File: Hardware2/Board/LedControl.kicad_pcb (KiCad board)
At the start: 2 copper layers, 69 x 50 mm, 124 parts, among them J2 Jumper, J3 Jumper, J4 J, J5 J, J6 J, P1 USB_OTG, P10 TP, P11 2059-302, P12 DISPLAY, P13 TP, P14 Conn_01x03, P15 TP, P16 2059-302, P17 2059-302, P18 CONN_01X03, P19 CONN_01X03, P2 TP, P20 TP, P21 TP, P22 TP, P23 TP, P24 2060-452, P25 2060-452, P26 TP, P27 TP, P28 2060-452, P29 2059-302, P3 TP, P30 LED_Strip, P31 LED_Strip, P32 TP, P33 TP, P34 TP, P4 TP, P5 2059-302, P6 TP, P7 TP, P8 Micro_SD, P9 TP, SW1 PEC12R-4215F-S0024, SW2 PEC12R-4215F-S0024, U1 STM32L433CCUx, U2 SP485CN, U3 SP485CN, U4 SP485CN, U5 TPS82130, U6 LP2985IM5-3.3, U7 TPS82130, U8 SP485CN, U9 TPS82130, X1 IQXO/7X

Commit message: LED strip power supply below strip
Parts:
- removed the C11 at (75.3, 86.3)
- removed the C11 at (82.3, 86.3)
- removed the C11 at (89.3, 86.3)
- removed the C11 at (96.3, 86.3)
- removed the C11 at (103.2, 86.3)
- removed the C12 at (75.2, 92.2)
- removed the C12 at (82.2, 92.2)
- removed the C12 at (89.2, 92.2)
- removed the C12 at (96.2, 92.2)
- removed the C12 at (103.0, 92.2)
- removed the P31 at (72.1, 96.5)
- removed the P31 at (79.1, 96.5)
- removed the P31 at (86.1, 96.5)
- removed the P31 at (93.1, 96.5)
- removed the P31 at (100.0, 96.5)
- removed the R16 at (75.7, 94.2)
- removed the R16 at (82.7, 94.2)
- removed the R16 at (89.7, 94.2)
- removed the R16 at (96.7, 94.2)
- removed the R16 at (103.6, 94.2)
- removed the R17 at (75.7, 96.0)
- removed the R17 at (82.7, 96.0)
- removed the R17 at (89.7, 96.0)
- removed the R17 at (96.7, 96.0)
- removed the R17 at (103.6, 96.0)
- removed the U9 at (74.9, 89.3)
- removed the U9 at (81.9, 89.3)
- removed the U9 at (88.9, 89.3)
- removed the U9 at (95.9, 89.3)
- removed the U9 at (102.8, 89.3)
- added C11: 10u, Capacitor_SMD:C_1206_3216Metric, F.Cu at (75.6, 96.6)
- added C11: 10u, Capacitor_SMD:C_1206_3216Metric, F.Cu at (82.6, 96.6)
- added C11: 10u, Capacitor_SMD:C_1206_3216Metric, F.Cu at (89.6, 96.6)
- added C11: 10u, Capacitor_SMD:C_1206_3216Metric, F.Cu at (96.6, 96.6)
- added C11: 10u, Capacitor_SMD:C_1206_3216Metric, F.Cu at (103.6, 96.6)
- added C12: 22u, Capacitor_SMD:C_0805_2012Metric, F.Cu at (75.0, 90.6)
- added C12: 22u, Capacitor_SMD:C_0805_2012Metric, F.Cu at (82.0, 90.6)
- added C12: 22u, Capacitor_SMD:C_0805_2012Metric, F.Cu at (89.0, 90.6)
- added C12: 22u, Capacitor_SMD:C_0805_2012Metric, F.Cu at (96.0, 90.6)
- added C12: 22u, Capacitor_SMD:C_0805_2012Metric, F.Cu at (103.0, 90.6)
- added P31: LED_Strip, LedControl:LED_Strip, F.Cu at (72.0, 97.5)
- added P31: LED_Strip, LedControl:LED_Strip, F.Cu at (79.0, 97.5)
- added P31: LED_Strip, LedControl:LED_Strip, F.Cu at (86.0, 97.5)
- added P31: LED_Strip, LedControl:LED_Strip, F.Cu at (93.0, 97.5)
- added P31: LED_Strip, LedControl:LED_Strip, F.Cu at (100.0, 97.5)
- added R16: 52k3, Resistor_SMD:R_0603_1608Metric, F.Cu at (74.8, 88.9)
- added R16: 52k3, Resistor_SMD:R_0603_1608Metric, F.Cu at (81.8, 88.9)
- added R16: 52k3, Resistor_SMD:R_0603_1608Metric, F.Cu at (88.8, 88.9)
- added R16: 52k3, Resistor_SMD:R_0603_1608Metric, F.Cu at (95.8, 88.9)
- added R16: 52k3, Resistor_SMD:R_0603_1608Metric, F.Cu at (102.8, 88.9)
- added R17: 10k, Resistor_SMD:R_0603_1608Metric, F.Cu at (74.3, 86.8)
- added R17: 10k, Resistor_SMD:R_0603_1608Metric, F.Cu at (81.3, 86.8)
- added R17: 10k, Resistor_SMD:R_0603_1608Metric, F.Cu at (88.3, 86.8)
- added R17: 10k, Resistor_SMD:R_0603_1608Metric, F.Cu at (95.3, 86.8)
- added R17: 10k, Resistor_SMD:R_0603_1608Metric, F.Cu at (102.3, 86.8)
- added U9: TPS82130, LedControl:TPS82130, F.Cu at (75.2, 93.5)
- added U9: TPS82130, LedControl:TPS82130, F.Cu at (82.2, 93.5)
- added U9: TPS82130, LedControl:TPS82130, F.Cu at (89.2, 93.5)
- added U9: TPS82130, LedControl:TPS82130, F.Cu at (96.2, 93.5)
- added U9: TPS82130, LedControl:TPS82130, F.Cu at (103.2, 93.5)
- D2, D3: value SS 12L -> SD1206S020S1R0
- D4: value D -> SD1206S020S1R0
- DIVIDER2: value Divider_21mm -> Divider_22mm; footprint LedControl:Divider_21mm -> LedControl:Divider_22mm
- P14: value Conn_01x03 -> TMM-103-03-G-S
- P30: footprint LedControl:LED_Strip_Start -> LedControl:LED_Strip
- moved C11 10.3 mm to (110.6, 96.6), turned to 180 degrees
- moved C9 10.3 mm to (117.6, 96.6), turned to 180 degrees
- moved R17 9.29 mm to (109.3, 86.8), turned to 90 degrees
- moved U8 8.61 mm to (122.0, 86.8)
- moved P29 8.50 mm to (130.0, 87.0)
- moved R11 7.31 mm to (77.5, 122.9), turned to 0 degrees
- moved P28 5.50 mm to (128.0, 94.0)
- moved R16 5.36 mm to (109.8, 88.9), turned to 180 degrees
- moved U7 4.22 mm to (117.2, 93.5), turned to 180 degrees
- moved U9 4.22 mm to (110.2, 93.5), turned to 180 degrees
- moved R15 3.82 mm to (116.3, 86.8)
- moved R14 3.67 mm to (116.8, 88.9), turned to 180 degrees
- moved C10 2.01 mm to (117.0, 90.6), turned to 0 degrees
- moved C12 1.55 mm to (110.0, 90.6), turned to 0 degrees
- moved DIVIDER1 1.00 mm to (77.0, 99.0)
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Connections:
- C10 pad 1: Net-(C10-Pad1) -> +5VD
- C10 pad 2: Net-(C10-Pad2) -> GNDD
- C11 pad 2: Net-(C10-Pad2) -> GNDD
- C12 pad 1: Net-(C10-Pad1) -> +5VD
- C12 pad 2: Net-(C10-Pad2) -> GNDD
- C9 pad 2: Net-(C10-Pad2) -> GNDD
- P28 pad 1: Net-(C10-Pad2) -> Net-(C11-Pad1)
- P28 pad 2: Net-(C11-Pad1) -> GNDD
- P30 pad 1: Net-(C10-Pad2) -> Net-(C11-Pad1)
- P30 pad 2: Net-(P30-Pad2) -> GNDD
- P30 pad 3: Net-(C10-Pad1) -> GNDD
- P30 pad 4: Net-(C10-Pad2) -> Net-(P30-Pad4)
- P30 pad 5: Net-(C11-Pad1) -> +5VD
- P31 pad 1: Net-(C10-Pad2) -> Net-(C11-Pad1)
- P31 pad 2: Net-(P30-Pad2) -> GNDD
- P31 pad 3: Net-(C10-Pad1) -> GNDD
- P31 pad 4: Net-(C10-Pad2) -> Net-(P30-Pad4)
- P31 pad 5: Net-(C11-Pad1) -> +5VD
- R14 pad 1: Net-(C10-Pad1) -> +5VD
- R15 pad 2: Net-(C10-Pad2) -> GNDD
- R16 pad 1: Net-(C10-Pad1) -> +5VD
- R17 pad 2: Net-(C10-Pad2) -> GNDD
- U7 pad 3: Net-(C10-Pad2) -> GNDD
- U7 pad 4: Net-(C10-Pad1) -> +5VD
- U7 pad 5: Net-(C10-Pad1) -> +5VD
- U7 pad 9: Net-(C10-Pad2) -> GNDD
- U8 pad 1: Net-(P30-Pad2) -> Net-(P30-Pad4)
- U8 pad 2: Net-(C10-Pad2) -> GNDD
- U8 pad 3: Net-(C10-Pad2) -> GNDD
- U8 pad 4: Net-(C10-Pad2) -> GNDD
- U8 pad 5: Net-(C10-Pad2) -> GNDD
- U8 pad 8: Net-(C10-Pad1) -> +5VD
- U9 pad 3: Net-(C10-Pad2) -> GNDD
- U9 pad 4: Net-(C10-Pad1) -> +5VD
- U9 pad 5: Net-(C10-Pad1) -> +5VD
- U9 pad 9: Net-(C10-Pad2) -> GNDD
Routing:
- net Net-(C10-Pad2): track 149.8 -> 0.00 mm, vias 12 -> 0
- net GNDD: track 0.00 -> 127.2 mm, vias 0 -> 10
- net +5VD: track 0.00 -> 82.3 mm, vias 0 -> 1
- net (no net): track 434.8 -> 485.6 mm, vias 30 -> 15
- net Net-(C10-Pad1): track 49.3 -> 0.00 mm, vias 4 -> 0
- net Net-(P30-Pad4): track 0.00 -> 16.9 mm, vias 0 -> 1
- net Net-(P30-Pad2): track 13.6 -> 0.00 mm
- net Net-(C11-Pad1): track 48.2 -> 56.2 mm
- net ENC1_SW: track 121.5 -> 128.1 mm
- net Net-(R14-Pad2): track 3.02 -> 6.70 mm
- net Net-(R16-Pad2): track 14.5 -> 13.4 mm
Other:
- board size 69 x 50 mm -> 70 x 51 mm
- board text added: "B A GND VCC"

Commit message: Add CAN bus
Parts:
- removed the C11 at (75.6, 96.6)
- removed the C11 at (82.6, 96.6)
- removed the C11 at (89.6, 96.6)
- removed the C11 at (96.6, 96.6)
- removed the C11 at (103.6, 96.6)
- removed the C12 at (75.0, 90.6)
- removed the C12 at (82.0, 90.6)
- removed the C12 at (89.0, 90.6)
- removed the C12 at (96.0, 90.6)
- removed the C12 at (103.0, 90.6)
- removed J6: J, LedControl:Jumper
- removed the P10 at (98.2, 115.0)
- removed the P31 at (72.0, 97.5)
- removed the P31 at (79.0, 97.5)
- removed the P31 at (86.0, 97.5)
- removed the P31 at (93.0, 97.5)
- removed the P31 at (100.0, 97.5)
- removed the R16 at (74.8, 88.9)
- removed the R16 at (81.8, 88.9)
- removed the R16 at (88.8, 88.9)
- removed the R16 at (95.8, 88.9)
- removed the R16 at (102.8, 88.9)
- removed the R17 at (74.3, 86.8)
- removed the R17 at (81.3, 86.8)
- removed the R17 at (88.3, 86.8)
- removed the R17 at (95.3, 86.8)
- removed the R17 at (102.3, 86.8)
- removed SLOT: Slot_15x2mm, LedControl:Slot_15x2mm
- removed the U9 at (75.2, 93.5)
- removed the U9 at (82.2, 93.5)
- removed the U9 at (89.2, 93.5)
- removed the U9 at (96.2, 93.5)
- removed the U9 at (103.2, 93.5)
- added C11: 10u, Capacitor_SMD:C_1206_3216Metric, F.Cu at (76.6, 96.6)
- added C11: 10u, Capacitor_SMD:C_1206_3216Metric, F.Cu at (83.4, 96.6)
- added C11: 10u, Capacitor_SMD:C_1206_3216Metric, F.Cu at (90.2, 96.6)
- added C11: 10u, Capacitor_SMD:C_1206_3216Metric, F.Cu at (97.0, 96.6)
- added C11: 10u, Capacitor_SMD:C_1206_3216Metric, F.Cu at (103.8, 96.6)
- added C12: 22u, Capacitor_SMD:C_0805_2012Metric, F.Cu at (76.2, 90.6)
- added C12: 22u, Capacitor_SMD:C_0805_2012Metric, F.Cu at (83.0, 90.6)
- added C12: 22u, Capacitor_SMD:C_0805_2012Metric, F.Cu at (89.8, 90.6)
- added C12: 22u, Capacitor_SMD:C_0805_2012Metric, F.Cu at (96.6, 90.6)
- added C12: 22u, Capacitor_SMD:C_0805_2012Metric, F.Cu at (103.4, 90.6)
- added C15: 100n, Capacitor_SMD:C_0603_1608Metric, F.Cu at (128.6, 112.2)
- added C16: 100n, Capacitor_SMD:C_0603_1608Metric, B.Cu at (111.1, 118.7)
- added C17: 100n, Capacitor_SMD:C_0603_1608Metric, B.Cu at (109.6, 118.7)
- added D5: SD1206S020S1R0, Diode_SMD:D_1206_3216Metric, B.Cu at (96.2, 113.8)
- added D6: SD1206S020S1R0, Diode_SMD:D_1206_3216Metric, B.Cu at (98.6, 111.2)
- added J7: Jumper, LedControl:Jumper, B.Cu at (77.0, 113.7)
- added P31: LED_Strip, LedControl:LED_Strip, F.Cu at (73.2, 97.5)
- added P31: LED_Strip, LedControl:LED_Strip, F.Cu at (80.0, 97.5)
- added P31: LED_Strip, LedControl:LED_Strip, F.Cu at (86.8, 97.5)
- added P31: LED_Strip, LedControl:LED_Strip, F.Cu at (93.6, 97.5)
- added P31: LED_Strip, LedControl:LED_Strip, F.Cu at (100.4, 97.5)
- added P35: 2060-452, LedControl:WAGO_2060-452, F.Cu at (69.0, 90.9)
- added P36: TP, LedControl:Pad, B.Cu at (93.8, 131.6)
- added P38: TP, LedControl:Pad, B.Cu at (100.8, 104.3)
- added P39: TP, LedControl:Pad, B.Cu at (100.1, 133.2)
- added P40: TP, LedControl:Pad, B.Cu at (102.2, 104.3)
- added P41: TP, LedControl:Pad, B.Cu at (76.6, 130.8)
- added P42: TP, LedControl:Pad, B.Cu at (76.6, 132.4)
- added P43: TP, LedControl:Pad, B.Cu at (76.6, 134.0)
- added P44: TP, LedControl:Pad, B.Cu at (98.0, 104.3)
- added P8: 2059-302, LedControl:WAGO_2059-302, F.Cu at (68.0, 105.0)
- added Q1: DMG1012UW, Package_TO_SOT_SMD:SOT-323_SC-70, B.Cu at (99.0, 115.2)
- added Q2: DMG1012UW, Package_TO_SOT_SMD:SOT-323_SC-70, B.Cu at (101.4, 112.6)
- added R16: 52k3, Resistor_SMD:R_0603_1608Metric, F.Cu at (76.0, 88.9)
- added R16: 52k3, Resistor_SMD:R_0603_1608Metric, F.Cu at (82.8, 88.9)
- added R16: 52k3, Resistor_SMD:R_0603_1608Metric, F.Cu at (89.6, 88.9)
- added R16: 52k3, Resistor_SMD:R_0603_1608Metric, F.Cu at (96.4, 88.9)
- added R16: 52k3, Resistor_SMD:R_0603_1608Metric, F.Cu at (103.2, 88.9)
- added R17: 10k, Resistor_SMD:R_0603_1608Metric, F.Cu at (75.5, 86.8)
- added R17: 10k, Resistor_SMD:R_0603_1608Metric, F.Cu at (82.3, 86.8)
- added R17: 10k, Resistor_SMD:R_0603_1608Metric, F.Cu at (89.1, 86.8)
- added R17: 10k, Resistor_SMD:R_0603_1608Metric, F.Cu at (95.9, 86.8)
- added R17: 10k, Resistor_SMD:R_0603_1608Metric, F.Cu at (102.7, 86.8)
- added R22: 390R, Resistor_SMD:R_0603_1608Metric, F.Cu at (111.6, 121.1)
- added R23: 120R, Resistor_SMD:R_1206_3216Metric, B.Cu at (92.0, 109.0)
- added R24: 120R, Resistor_SMD:R_1206_3216Metric, B.Cu at (92.0, 111.2)
- added R25: 10k, Resistor_SMD:R_0603_1608Metric, B.Cu at (110.4, 111.1)
- added R26: 120R, Resistor_SMD:R_1206_3216Metric, B.Cu at (110.7, 114.9)
- added R27: 10k, Resistor_SMD:R_0603_1608Metric, B.Cu at (108.8, 111.1)
- added R28: 120R, Resistor_SMD:R_1206_3216Metric, B.Cu at (108.5, 114.9)
- added R29: 10k, Resistor_SMD:R_0603_1608Metric, F.Cu at (128.2, 129.0)
- added U10: SP485CN, Package_SO:SOIC-8_3.9x4.9mm_P1.27mm, B.Cu at (92.0, 104.1)
- added U9: TPS82130, LedControl:TPS82130, F.Cu at (76.4, 93.5)
- added U9: TPS82130, LedControl:TPS82130, F.Cu at (83.2, 93.5)
- added U9: TPS82130, LedControl:TPS82130, F.Cu at (90.0, 93.5)
- added U9: TPS82130, LedControl:TPS82130, F.Cu at (96.8, 93.5)
- added U9: TPS82130, LedControl:TPS82130, F.Cu at (103.6, 93.5)
- J2: footprint LedControl:Jumper3 -> LedControl:Jumper; moved to F.Cu
- J3: footprint LedControl:Jumper -> LedControl:Jumper3; moved to F.Cu
- J4, J5: value J -> Jumper; footprint LedControl:Jumper -> LedControl:Jumper3; moved to B.Cu
- P11: value 2059-302 -> Header; footprint LedControl:WAGO_2059-302 -> Connector_PinHeader_2.54mm:PinHeader_1x04_P2.54mm_Vertical
- P14, P18, SW1, SW2: moved to F.Cu
- P15, P17, R5, U3: moved to B.Cu
- P16: value 2059-302 -> TP; footprint LedControl:WAGO_2059-302 -> LedControl:Pad; moved to B.Cu
- P19: value CONN_01X03 -> TP; footprint Connector_PinHeader_2.54mm:PinHeader_1x03_P2.54mm_Vertical -> LedControl:Pad
- P2, P3, P4: value TP -> 2059-302; footprint LedControl:Pad -> LedControl:WAGO_2059-302; moved to F.Cu
- P6, P7, P9: value TP -> 2059-302; footprint LedControl:Pad -> LedControl:WAGO_2059-302
- R19: value 52k3 -> 10k
- R20: value 10k -> 52k3
- R4, R6: value 120R -> 390R; footprint Resistor_SMD:R_1206_3216Metric -> Resistor_SMD:R_0603_1608Metric; moved to B.Cu
- R8: value 120R -> 10k; footprint Resistor_SMD:R_1206_3216Metric -> Resistor_SMD:R_0603_1608Metric
- U2: value SP485CN -> SN65HVD230
- moved C1 55.8 mm to (70.2, 129.0), turned to 180 degrees
- moved R10 52.0 mm to (66.2, 118.8), turned to 90 degrees
- moved P14 49.8 mm to (129.8, 133.8), turned to 90 degrees
- moved J4 49.1 mm to (125.1, 113.4), turned to 270 degrees
- moved U4 48.1 mm to (71.2, 132.4), turned to 180 degrees
- moved R9 45.4 mm to (68.4, 118.8), turned to 90 degrees
- moved P19 44.4 mm to (114.8, 130.9)
- moved R11 40.8 mm to (117.4, 131.5), turned to 180 degrees
- moved P4 37.1 mm to (120.0, 105.0), turned to 270 degrees
- moved P17 34.0 mm to (80.0, 105.0)
- moved P6 31.7 mm to (114.0, 105.0), turned to 270 degrees
- moved P18 30.2 mm to (67.2, 123.2), turned to 0 degrees
- moved P3 27.0 mm to (126.0, 105.0), turned to 270 degrees
- moved P7 26.5 mm to (120.0, 105.0), turned to 270 degrees
- moved P2 26.2 mm to (114.0, 105.0)
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- renumbered P8 to P10
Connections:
- J2 pad 1: +3V3 -> GND
- J3 pad 2: Net-(J3-Pad2) -> +3V3
- J4 pad 1: Net-(D2-Pad2) -> Net-(J4-Pad1)
- J4 pad 2: VCC -> +3V3
- J5 pad 1: Net-(D3-Pad2) -> Net-(J5-Pad1)
- J5 pad 2: VCC -> +3V3
- P11 pad 1: Net-(J3-Pad1) -> GND
- P11 pad 2: Net-(P11-Pad2) -> SWDIO
- P14 pad 1: SWDCLK -> GND
- P14 pad 3: GND -> SWCLK
- P17 pad 1: Net-(P17-Pad1) -> Net-(J5-Pad1)
- P17 pad 2: Net-(P17-Pad2) -> GND
- P19 pad 1: GND -> Net-(P19-Pad1)
- P2 pad 1: Net-(P2-Pad1) -> CANL
- P21 pad 1: +3V3 -> +5V
- P22 pad 1: +5V -> +3V3
- P3 pad 1: Net-(P3-Pad1) -> CANL
- P4 pad 1: Net-(P4-Pad1) -> GND
- P5 pad 2: Net-(J2-Pad2) -> Net-(J3-Pad1)
- P6 pad 1: Net-(P6-Pad1) -> RS485A
- P7 pad 1: Net-(P7-Pad1) -> Net-(J4-Pad1)
- P9 pad 1: DISP_SCK -> STRIP2_A
- R10 pad 2: Net-(P17-Pad1) -> STRIP1_A
- R19 pad 1: Net-(D3-Pad2) -> U1
- R19 pad 2: U2 -> GND
- R2 pad 1: Net-(J3-Pad2) -> CANH
- R2 pad 2: Net-(P11-Pad2) -> CANL
- R20 pad 1: U1 -> Net-(D3-Pad2)
- R20 pad 2: GND -> U2
- R4 pad 1: Net-(P16-Pad1) -> +5V
- R4 pad 2: Net-(R4-Pad2) -> RS485A
- R5 pad 1: Net-(P16-Pad1) -> RS485A
- R5 pad 2: Net-(P16-Pad2) -> RS485B
- R6 pad 1: Net-(P16-Pad2) -> RS485B
- R6 pad 2: Net-(R6-Pad2) -> GND
- R8 pad 1: DEBUG_LED -> Net-(J2-Pad2)
- R8 pad 2: Net-(D1-Pad2) -> GND
- R9 pad 2: Net-(P17-Pad2) -> STRIP1_B
- SW1 pad : (no net) -> GND
- SW1 pad A: ENC1_CH2 -> ENC1_CH1
- SW1 pad B: ENC1_CH1 -> ENC1_CH2
- SW1 pad S1: +3V3 -> ENC1_SW
- SW1 pad S2: ENC1_SW -> +3V3
- SW2 pad : (no net) -> GND
- SW2 pad A: ENC2_CH2 -> ENC2_CH1
- SW2 pad B: ENC2_CH1 -> ENC2_CH2
- U1 pad 13: STRIP2_RX -> Net-(P13-Pad1)
- U1 pad 14: Net-(P13-Pad1) -> DEBUG_LED
- U1 pad 2: STRIP2_DE -> Net-(P19-Pad1)
- U1 pad 37: SWDCLK -> SWCLK
- U1 pad 39: Net-(P4-Pad1) -> Net-(P36-Pad1)
- U1 pad 40: Net-(P6-Pad1) -> Net-(P39-Pad1)
- U1 pad 45: Net-(P7-Pad1) -> CAN_RX
- U1 pad 46: DEBUG_LED -> CAN_TX
- U1 pad 6: Net-(P2-Pad1) -> Net-(P16-Pad1)
- U1 pad 7: Net-(P3-Pad1) -> NRST
- U2 pad 1: RS485_RX -> CAN_TX
- U2 pad 2: RS485_DE -> GND
- U2 pad 3: RS485_DE -> +3V3
- U2 pad 4: RS485_TX -> CAN_RX
- U2 pad 5: GND -> Net-(U2-Pad5)
- U2 pad 6: Net-(J3-Pad1) -> CANL
- U2 pad 7: Net-(P11-Pad2) -> CANH
- U2 pad 8: +5V -> Net-(J2-Pad2)
- U3 pad 1: STRIP2_RX -> RS485_RX
- U3 pad 2: STRIP2_DE -> RS485_DE
- U3 pad 3: STRIP2_DE -> RS485_DE
- U3 pad 4: STRIP2_TX -> RS485_TX
- U3 pad 6: Net-(R4-Pad2) -> RS485A
- U3 pad 7: Net-(R6-Pad2) -> RS485B
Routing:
- net ENC1_SW: track 128.1 -> 59.6 mm
- net STRIP2_TX: track 9.06 -> 59.0 mm, vias 0 -> 1
- net +5V: track 121.2 -> 169.0 mm, vias 7 -> 10
- net CAN_RX: track 0.00 -> 46.3 mm, vias 0 -> 2
- net CAN_TX: track 0.00 -> 41.0 mm, vias 0 -> 2
- net SWCLK: track 0.00 -> 40.0 mm, vias 0 -> 1
- net NRST: track 0.00 -> 34.3 mm, vias 0 -> 2
- net CANH: track 0.00 -> 33.7 mm, vias 0 -> 2
- net RS485B: track 0.00 -> 32.2 mm, vias 0 -> 2
- net SWDCLK: track 31.4 -> 0.00 mm, vias 2 -> 0
- net CANL: track 0.00 -> 31.4 mm
- net STRIP1_TTY_TX: track 66.6 -> 39.7 mm
- net GNDD: track 127.2 -> 153.8 mm, vias 10 -> 12
- net Net-(C11-Pad1): track 56.2 -> 82.7 mm, vias 3 -> 6
- net RS485A: track 0.00 -> 24.7 mm
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- removed copper zone on B.Cu, net Net-(D2-Pad2)
- removed copper zone on B.Cu, net Net-(D3-Pad2)
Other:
- board text added: "A B"
- board text added: "CAN H L"
- board text added: "D CL"
- board text added: "GND VCC"
- board text added: "R CL D"
- board text added: "RS485 B A"
- board text added: "STRIP2 B A GND 5V"
- board text added: "VCC G VCC GND"
- board text removed: "B A B A B A LED1 LED2 485"
- board text removed: "RS485 TERM"
- board text removed: "VCC GND VCC GND"
- board text removed: "VDD"

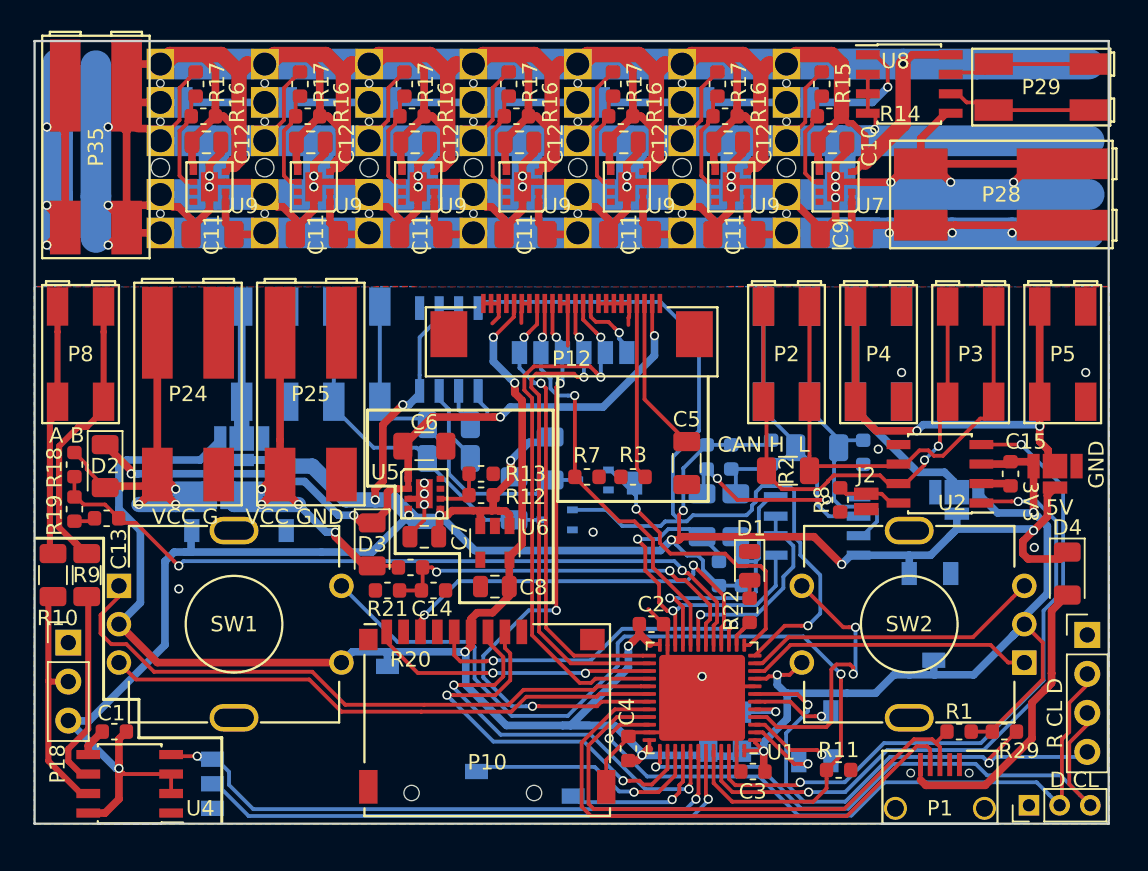
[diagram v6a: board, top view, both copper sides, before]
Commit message: USB and SD card at center
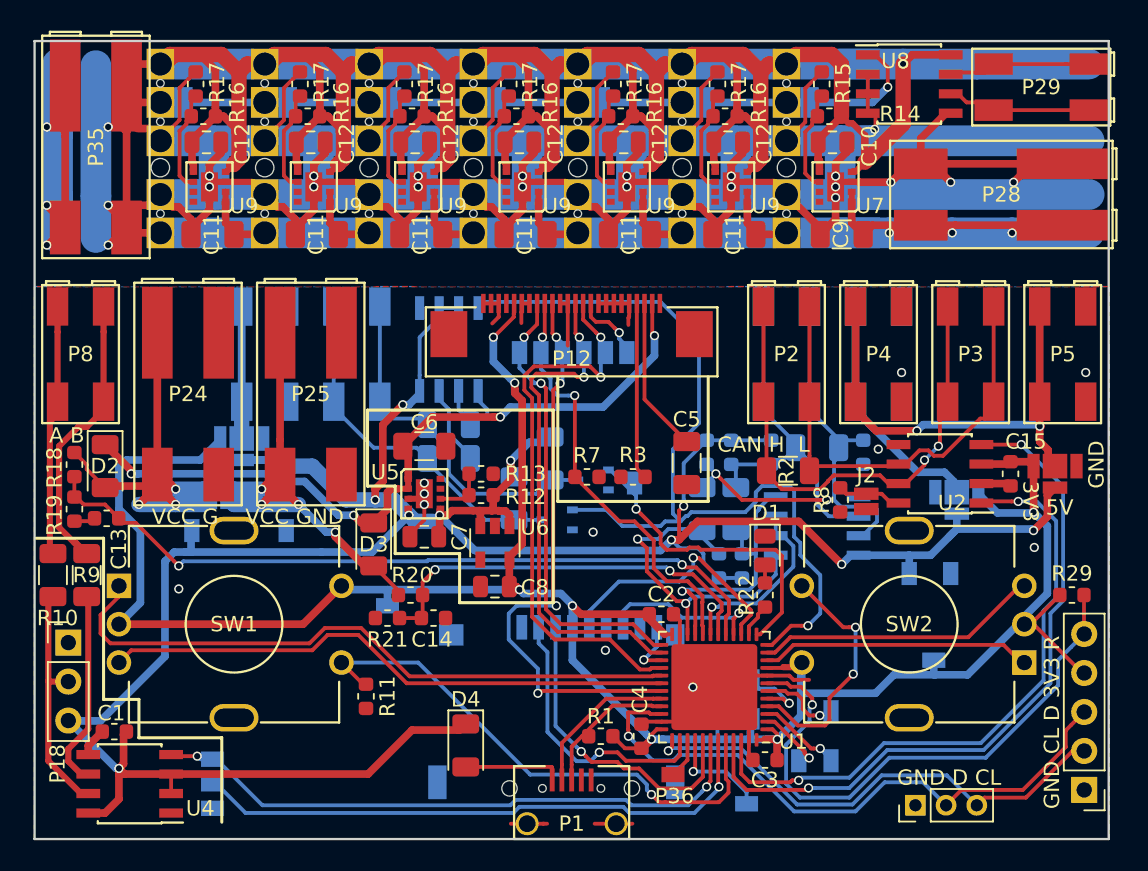
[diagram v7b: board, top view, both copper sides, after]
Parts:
- P10: moved to B.Cu
- P11: footprint Connector_PinHeader_2.54mm:PinHeader_1x04_P2.54mm_Vertical -> Connector_PinHeader_2.54mm:PinHeader_1x05_P2.54mm_Vertical
- P36: moved to F.Cu
- moved D4 40.8 mm to (93.1, 129.9)
- moved R11 31.2 mm to (86.6, 126.7), turned to 90 degrees
- moved P1 24.0 mm to (100.0, 135.0)
- moved R1 23.4 mm to (101.9, 129.3)
- moved P36 12.8 mm to (106.6, 131.8)
- moved P39 11.3 mm to (111.4, 133.7)
- moved P11 10.1 mm to (133.4, 132.8), turned to 180 degrees
- moved R29 9.93 mm to (132.6, 120.1)
- moved P14 7.40 mm to (122.4, 133.8)
- moved P10 4.55 mm to (99.0, 132.3), turned to 180 degrees
- moved P22 3.95 mm to (88.0, 120.8)
- moved X1 2.17 mm to (110.5, 126.9)
- moved C14 1.80 mm to (91.0, 121.6)
- moved R20 1.80 mm to (89.5, 120.1)
- moved R21 1.80 mm to (88.0, 121.6)
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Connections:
- P11 pad 2: SWDIO -> SWCLK
- P11 pad 3: SWCLK -> SWDIO
- P11 pad 4: NRST -> +3V3
- SW1 pad S1: ENC1_SW -> +3V3
- SW1 pad S2: +3V3 -> ENC1_SW
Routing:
- net USB_DP: track 35.5 -> 9.60 mm
- net USB_DM: track 35.4 -> 10.1 mm
- net ENC1_SW: track 59.6 -> 35.2 mm
- net +5V: track 169.0 -> 185.8 mm
- net SD_MISO: track 26.5 -> 10.8 mm, vias 2 -> 1
- net SD_DET: track 18.7 -> 3.64 mm, vias 2 -> 1
- net Net-(D4-Pad2): track 20.4 -> 6.46 mm
- net Net-(P36-Pad1): track 15.5 -> 2.66 mm, vias 1 -> 0
- net GND: track 50.2 -> 41.7 mm, vias 10 -> 11
- net SD_NSS: track 26.2 -> 18.1 mm, vias 2 -> 1
- net SWCLK: track 40.0 -> 32.6 mm
- net +3V3: track 171.4 -> 164.1 mm, vias 8 -> 7
- net SD_MOSI: track 27.7 -> 20.4 mm, vias 2 -> 1
- net SD_SCK: track 22.4 -> 16.7 mm, vias 2 -> 1
- net SWDIO: track 45.4 -> 40.4 mm
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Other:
- board size 70 x 51 mm -> 70 x 52 mm
- board text added: "GND CL D 3V3 R"
- board text added: "GND D CL"
- board text removed: "D CL"
- board text removed: "R CL D"
